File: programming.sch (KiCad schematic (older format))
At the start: 2 parts

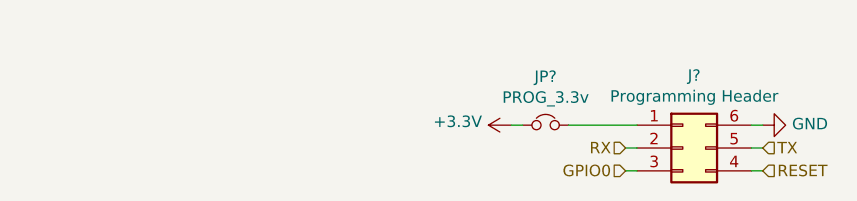
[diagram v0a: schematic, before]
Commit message: Added LAN circuit
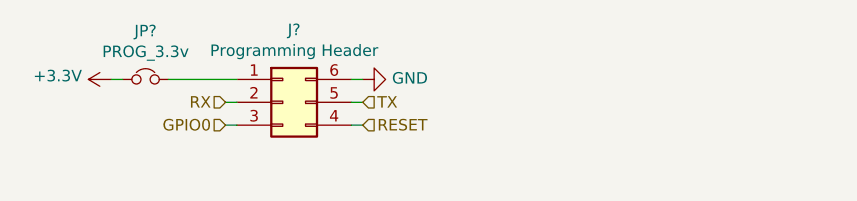
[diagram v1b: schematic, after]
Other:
- moved on the sheet: J?, JP?
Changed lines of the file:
@@
 $Descr A4 11693 8268
 encoding utf-8
-Sheet 5 5
-Title ""
-Date ""
-Rev ""
-Comp ""
-Comment1 ""
-Comment2 ""
+Sheet 5 6
+Title "ESP Expander"
+Date "2022-02-20"
+Rev "0.1"
+Comp "Silard Gal"
+Comment1 "https://github.com/silardg/esp-expander"
+Comment2 "https://www.linkedin.com/in/silard-gal/"
 Comment3 ""
 Comment4 ""
 $EndDescr
-$Comp
-L Connector_Generic:Conn_02x03_Counter_Clockwise J?
-U 1 1 621750AB
-P 5650 3850
-F 0 "J?" H 5700 4167 50  0000 C CNN
-F 1 "Programming Header" H 5700 4076 50  0000 C CNN
-F 2 "Connector:Tag-Connect_TC2030-IDC-NL_2x03_P1.27mm_Vertical" H 5650 3850 50  0001 C CNN
-F 3 "~" H 5650 3850 50  0001 C CNN
-	1    5650 3850
-	1    0    0    -1
-$EndComp
+Text HLabel 3650 3650 0    50   Input ~ 0
+RX
+Text HLabel 4250 3650 2    50   Input ~ 0
+TX
+Text HLabel 3650 3750 0    50   Input ~ 0
+GPIO0
+Text HLabel 4250 3750 2    50   Input ~ 0
+RESET
+Wire Wire Line
+	3650 3650 3700 3650
+Wire Wire Line
+	3650 3750 3700 3750
+Wire Wire Line
+	4200 3650 4250 3650
+Wire Wire Line
+	4200 3750 4250 3750
+Wire Wire Line
+	3150 3550 3200 3550
+Wire Wire Line
+	3400 3550 3700 3550
+Wire Wire Line
+	4200 3550 4250 3550
 $Comp
 L power:+3.3V #PWR?
 U 1 1 621758D0
-P 4900 3750
-F 0 "#PWR?" H 4900 3600 50  0001 C CNN
-F 1 "+3.3V" V 4915 3878 50  0000 L CNN
-F 2 "" H 4900 3750 50  0001 C CNN
-F 3 "" H 4900 3750 50  0001 C CNN
-	1    4900 3750
+P 3150 3550
+F 0 "#PWR?" H 3150 3400 50  0001 C CNN
+F 1 "+3.3V" V 3165 3678 50  0000 L CNN
+F 2 "" H 3150 3550 50  0001 C CNN
+F 3 "" H 3150 3550 50  0001 C CNN
+	1    3150 3550
+	0    -1   -1   0
+$EndComp
+$Comp
+L power:GND #PWR?
+U 1 1 6217836E
+P 4250 3550
+F 0 "#PWR?" H 4250 3300 50  0001 C CNN
+F 1 "GND" V 4255 3422 50  0000 R CNN
+F 2 "" H 4250 3550 50  0001 C CNN
+F 3 "" H 4250 3550 50  0001 C CNN
+	1    4250 3550
 	0    -1   -1   0
 $EndComp
@@
 L Device:Jumper_NC_Small JP?
 U 1 1 62176604
-P 5050 3750
-F 0 "JP?" H 5050 3962 50  0000 C CNN
-F 1 "PROG_3.3v" H 5050 3871 50  0000 C CNN
-F 2 "Jumper:SolderJumper-2_P1.3mm_Bridged_Pad1.0x1.5mm" H 5050 3750 50  0001 C CNN
-F 3 "~" H 5050 3750 50  0001 C CNN
-	1    5050 3750
+P 3300 3550
+F 0 "JP?" H 3300 3762 50  0000 C CNN
+F 1 "PROG_3.3v" H 3300 3671 50  0000 C CNN
+F 2 "Jumper:SolderJumper-2_P1.3mm_Bridged_Pad1.0x1.5mm" H 3300 3550 50  0001 C CNN
+F 3 "~" H 3300 3550 50  0001 C CNN
+	1    3300 3550
 	1    0    0    -1
 $EndComp
 $Comp
-L power:GND #PWR?
-U 1 1 6217836E
-P 6000 3750
-F 0 "#PWR?" H 6000 3500 50  0001 C CNN
-F 1 "GND" V 6005 3622 50  0000 R CNN
-F 2 "" H 6000 3750 50  0001 C CNN
-F 3 "" H 6000 3750 50  0001 C CNN
-	1    6000 3750
-	0    -1   -1   0
+L Connector_Generic:Conn_02x03_Counter_Clockwise J?
+U 1 1 621750AB
+P 3900 3650
+F 0 "J?" H 3950 3967 50  0000 C CNN
+F 1 "Programming Header" H 3950 3876 50  0000 C CNN
+F 2 "Connector:Tag-Connect_TC2030-IDC-NL_2x03_P1.27mm_Vertical" H 3900 3650 50  0001 C CNN
+F 3 "~" H 3900 3650 50  0001 C CNN
+	1    3900 3650
+	1    0    0    -1
 $EndComp
-Text HLabel 5400 3850 0    50   Input ~ 0
-RX
-Text HLabel 6000 3850 2    50   Input ~ 0
-TX
-Text HLabel 5400 3950 0    50   Input ~ 0
-GPIO0
-Text HLabel 6000 3950 2    50   Input ~ 0
-RESET
-Wire Wire Line
-	5400 3850 5450 3850
-Wire Wire Line
-	5400 3950 5450 3950
-Wire Wire Line
-	5950 3850 6000 3850
-Wire Wire Line
-	5950 3950 6000 3950
-Wire Wire Line
-	5950 3750 6000 3750
-Wire Wire Line
-	5150 3750 5450 3750
-Wire Wire Line
-	4900 3750 4950 3750
 $EndSCHEMATC

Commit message: Exported first net
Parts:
- gave numbers to parts that had none: 2
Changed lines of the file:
@@
 	4200 3550 4250 3550
 $Comp
-L power:+3.3V #PWR?
+L power:+3.3V #PWR0125
 U 1 1 621758D0
 P 3150 3550
-F 0 "#PWR?" H 3150 3400 50  0001 C CNN
+F 0 "#PWR0125" H 3150 3400 50  0001 C CNN
 F 1 "+3.3V" V 3165 3678 50  0000 L CNN
 F 2 "" H 3150 3550 50  0001 C CNN
@@
 $EndComp
 $Comp
-L power:GND #PWR?
+L power:GND #PWR0126
 U 1 1 6217836E
 P 4250 3550
-F 0 "#PWR?" H 4250 3300 50  0001 C CNN
+F 0 "#PWR0126" H 4250 3300 50  0001 C CNN
 F 1 "GND" V 4255 3422 50  0000 R CNN
 F 2 "" H 4250 3550 50  0001 C CNN
@@
 $EndComp
 $Comp
-L Device:Jumper_NC_Small JP?
+L Device:Jumper_NC_Small JP1
 U 1 1 62176604
 P 3300 3550
-F 0 "JP?" H 3300 3762 50  0000 C CNN
+F 0 "JP1" H 3300 3762 50  0000 C CNN
 F 1 "PROG_3.3v" H 3300 3671 50  0000 C CNN
 F 2 "Jumper:SolderJumper-2_P1.3mm_Bridged_Pad1.0x1.5mm" H 3300 3550 50  0001 C CNN
@@
 $EndComp
 $Comp
-L Connector_Generic:Conn_02x03_Counter_Clockwise J?
+L Connector_Generic:Conn_02x03_Counter_Clockwise J1
 U 1 1 621750AB
 P 3900 3650
-F 0 "J?" H 3950 3967 50  0000 C CNN
+F 0 "J1" H 3950 3967 50  0000 C CNN
 F 1 "Programming Header" H 3950 3876 50  0000 C CNN
 F 2 "Connector:Tag-Connect_TC2030-IDC-NL_2x03_P1.27mm_Vertical" H 3900 3650 50  0001 C CNN
